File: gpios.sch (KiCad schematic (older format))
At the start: 28 parts, among them J1 TB_1X3, J2 TB_1X2, J3 TB_1X2, Q1 BC548, Q2 BC548, U1 4N25, U2 LM35, U3 4N25, U4 RELAY, U5 RELAY

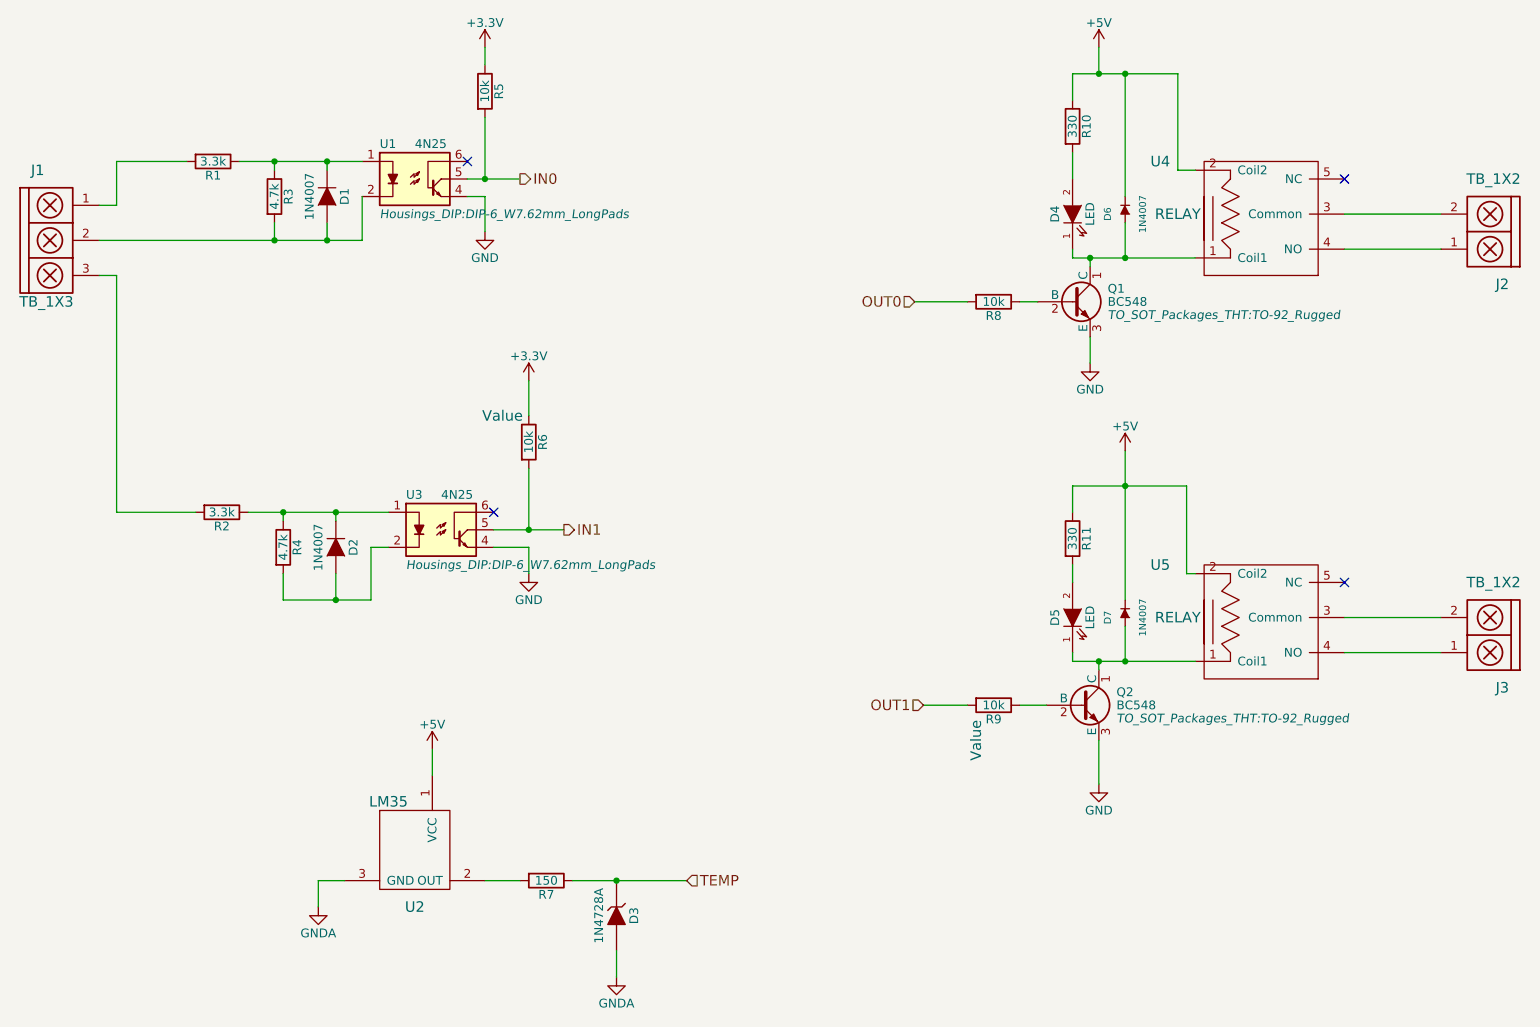
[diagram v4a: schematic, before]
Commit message: correcciones en esquemarico. ERC OK. Se crearon rotulos. PCB: replacing mas compacto
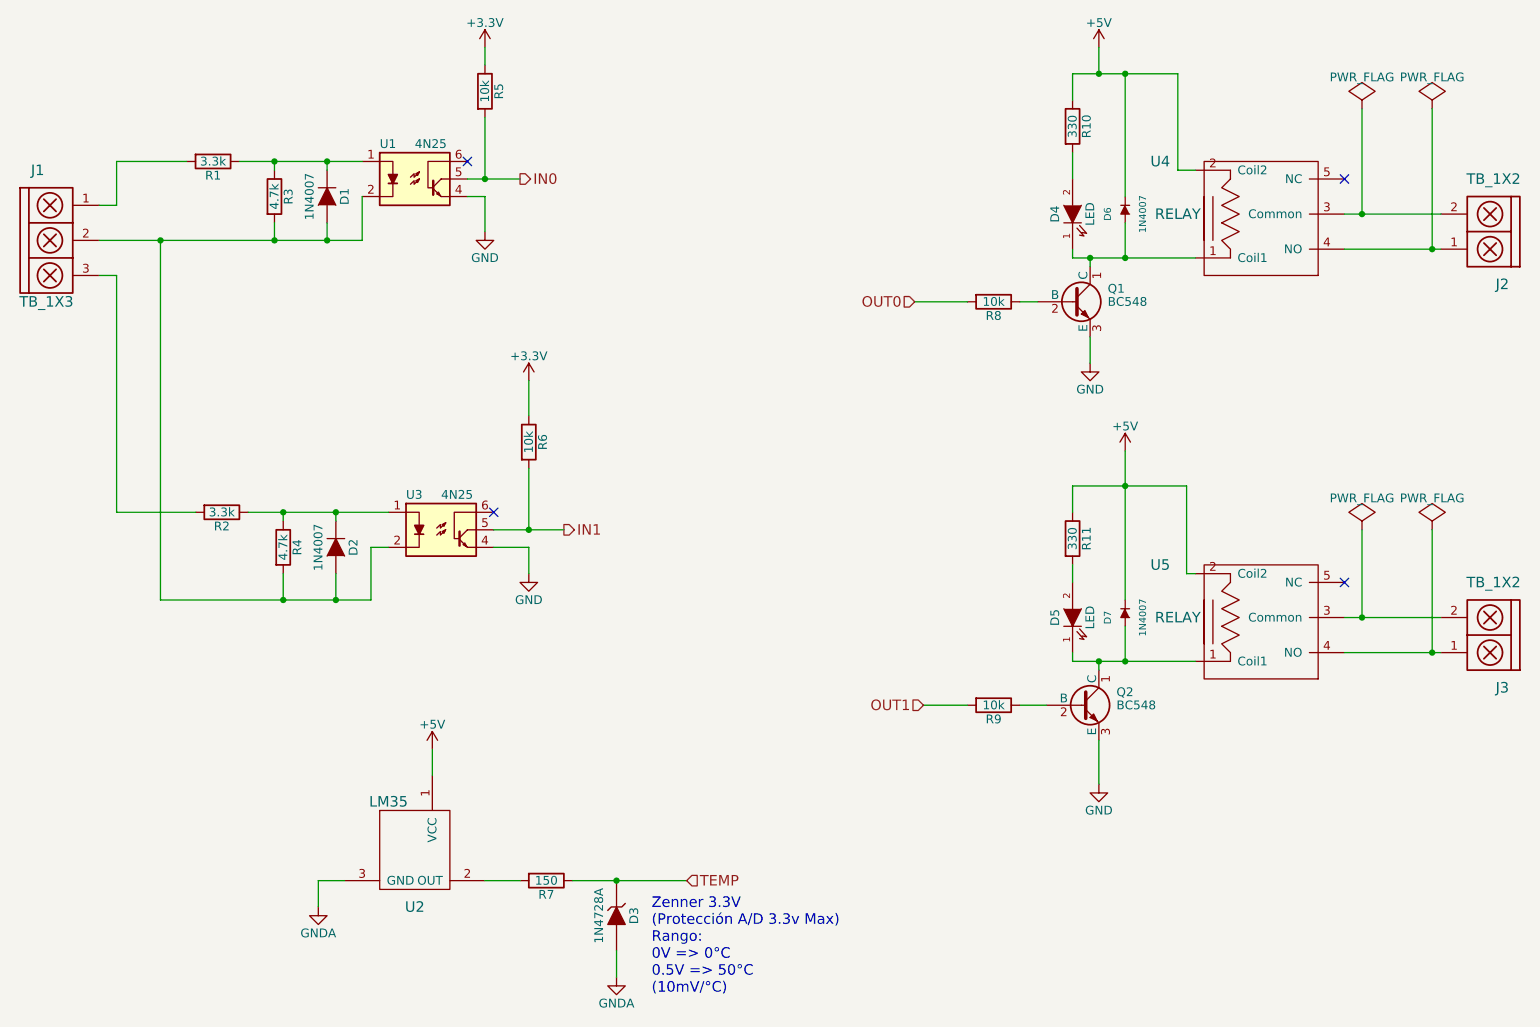
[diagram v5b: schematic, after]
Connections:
- net at D1.2 (A), J1.2, R3.2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: now also D2.2 (A), R4.2, U3.2
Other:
- note added: "Zenner 3.3V\n(Protección A/D 3.3v Max)\nRango: \n0V => 0°C\n0.5V => 50°C\n(10mV/°C)"
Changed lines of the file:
@@
 encoding utf-8
 Sheet 2 4
-Title "Poncho EDU-CIAA-NXP IoT"
+Title "Poncho EDU-CIAA-NXP IoT. GPIOs"
 Date "2016-11-09"
 Rev "1"
@@
 F 0 "Q1" H 7400 2525 50  0000 L CNN
 F 1 "BC548" H 7400 2450 50  0000 L CNN
-F 2 "TO_SOT_Packages_THT:TO-92_Rugged" H 7400 2375 50  0000 L CIN
+F 2 "TO_SOT_Packages_THT:TO-92_Rugged" H 7400 2375 50  0001 L CIN
 F 3 "" H 7200 2450 50  0000 L CNN
 	1    7200 2450
@@
 F 0 "Q2" H 7450 4825 50  0000 L CNN
 F 1 "BC548" H 7450 4750 50  0000 L CNN
-F 2 "TO_SOT_Packages_THT:TO-92_Rugged" H 7450 4675 50  0000 L CIN
+F 2 "TO_SOT_Packages_THT:TO-92_Rugged" H 7450 4675 50  0001 L CIN
 F 3 "" H 7250 4750 50  0000 L CNN
 	1    7250 4750
@@
 F 2 "Resistors_THT:Resistor_Horizontal_RM7mm" V 6680 4750 50  0001 C CNN
 F 3 "" H 6750 4750 50  0000 C CNN
-F 4 "Value" H 6950 4650 60  0000 C CNN "Digikey"
+F 4 "Value" H 6950 4650 60  0001 C CNN "Digikey"
 F 5 "Value" H 6750 4750 60  0001 C CNN "Fieldname"
 	1    6750 4750
@@
 F 0 "U1" H 3250 1950 50  0000 L CNN
 F 1 "4N25" H 3450 1950 50  0000 L CNN
-F 2 "Housings_DIP:DIP-6_W7.62mm_LongPads" H 3250 1550 50  0000 L CIN
+F 2 "Housings_DIP:DIP-6_W7.62mm_LongPads" H 3250 1550 50  0001 L CIN
 F 3 "" H 3450 1750 50  0000 L CNN
 	1    3450 1750
@@
 F 0 "U3" H 3400 3950 50  0000 L CNN
 F 1 "4N25" H 3600 3950 50  0000 L CNN
-F 2 "Housings_DIP:DIP-6_W7.62mm_LongPads" H 3400 3550 50  0000 L CIN
+F 2 "Housings_DIP:DIP-6_W7.62mm_LongPads" H 3400 3550 50  0001 L CIN
 F 3 "" H 3600 3750 50  0000 L CNN
 	1    3600 3750
@@
 F 2 "Resistors_THT:Resistor_Horizontal_RM7mm" V 4030 3250 50  0001 C CNN
 F 3 "" H 4100 3250 50  0000 C CNN
-F 4 "Value" H 3950 3400 60  0000 C CNN "Digikey"
+F 4 "Value" H 3950 3400 60  0001 C CNN "Digikey"
 F 5 "Value" H 4100 3250 60  0001 C CNN "Fieldname"
 	1    4100 3250
@@
 	3200 3850 3200 4150
 Wire Wire Line
-	3200 4150 2700 4150
+	3200 4150 2000 4150
 Wire Wire Line
 	2700 4150 2700 4000
@@
 	1    0    0    -1
 $EndComp
+Wire Wire Line
+	2000 4150 2000 2100
+Connection ~ 2000 2100
+Connection ~ 2700 4150
+Text Notes 4800 6400 0    60   ~ 0
+Zenner 3.3V\n(Protección A/D 3.3v Max)\nRango: \n0V => 0°C\n0.5V => 50°C\n(10mV/°C)
+$Comp
+L PWR_FLAG #FLG012
+U 1 1 582F3FFE
+P 8850 1350
+F 0 "#FLG012" H 8850 1445 50  0001 C CNN
+F 1 "PWR_FLAG" H 8850 1530 50  0000 C CNN
+F 2 "" H 8850 1350 50  0000 C CNN
+F 3 "" H 8850 1350 50  0000 C CNN
+	1    8850 1350
+	1    0    0    -1
+$EndComp
+$Comp
+L PWR_FLAG #FLG013
+U 1 1 582F404A
+P 9250 1350
+F 0 "#FLG013" H 9250 1445 50  0001 C CNN
+F 1 "PWR_FLAG" H 9250 1530 50  0000 C CNN
+F 2 "" H 9250 1350 50  0000 C CNN
+F 3 "" H 9250 1350 50  0000 C CNN
+	1    9250 1350
+	1    0    0    -1
+$EndComp
+Wire Wire Line
+	8850 1350 8850 1950
+Connection ~ 8850 1950
+Wire Wire Line
+	9250 1350 9250 2150
+Connection ~ 9250 2150
+$Comp
+L PWR_FLAG #FLG014
+U 1 1 582F58B7
+P 8850 3750
+F 0 "#FLG014" H 8850 3845 50  0001 C CNN
+F 1 "PWR_FLAG" H 8850 3930 50  0000 C CNN
+F 2 "" H 8850 3750 50  0000 C CNN
+F 3 "" H 8850 3750 50  0000 C CNN
+	1    8850 3750
+	1    0    0    -1
+$EndComp
+$Comp
+L PWR_FLAG #FLG015
+U 1 1 582F5903
+P 9250 3750
+F 0 "#FLG015" H 9250 3845 50  0001 C CNN
+F 1 "PWR_FLAG" H 9250 3930 50  0000 C CNN
+F 2 "" H 9250 3750 50  0000 C CNN
+F 3 "" H 9250 3750 50  0000 C CNN
+	1    9250 3750
+	1    0    0    -1
+$EndComp
+Wire Wire Line
+	8850 3750 8850 4250
+Connection ~ 8850 4250
+Wire Wire Line
+	9250 3750 9250 4450
+Connection ~ 9250 4450
 $EndSCHEMATC

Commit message: codigos digikey. falta terminar
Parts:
- D1, D2, D6, D7: Digikey# (none) -> 1N4007-TPMSTR-ND
- D4, D5: Digikey# (none) -> MV5054A3EL-ND
- Q1, Q2: Digikey# (none) -> BC548BTATB-ND
- R1: Digikey# (none) -> CF14JT3K30TR-ND; Fieldname Value -> (none)
- R10, R11: Digikey# (none) -> P330BATB-ND
- R2: Digikey# (none) -> CF14JT3K30TR-ND
- R3, R4: Digikey# (none) -> CF14JT4K70TR-ND
- R5, R6, R8, R9: Digikey# (none) -> CF14JT10K0TR-ND
- R7: Digikey# (none) -> CF14JT150RTR-ND
- U1, U3: Digikey# (none) -> 160-1300-5-ND; Fieldname (none) -> Value
- U2: Digikey# (none) -> LM35DZ/NOPB-ND
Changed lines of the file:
@@
 F 2 "TO_SOT_Packages_THT:TO-92_Rugged" H 7400 2375 50  0001 L CIN
 F 3 "" H 7200 2450 50  0000 L CNN
+F 4 "BC548BTATB-ND" H 7200 2450 60  0001 C CNN "Digikey#"
 	1    7200 2450
 	1    0    0    -1
@@
 F 2 "TO_SOT_Packages_THT:TO-92_Rugged" H 7450 4675 50  0001 L CIN
 F 3 "" H 7250 4750 50  0000 L CNN
+F 4 "BC548BTATB-ND" H 7250 4750 60  0001 C CNN "Digikey#"
 	1    7250 4750
 	1    0    0    -1
@@
 F 2 "Diodes_THT:Diode_DO-35_SOD27_Horizontal_RM10" H 7500 1950 60  0001 C CNN
 F 3 "" H 7500 1950 60  0000 C CNN
-F 4 "Value" H 7700 2000 60  0001 C CNN "Digikey"
-F 5 "Value" H 7500 1950 60  0001 C CNN "Fieldname"
+F 4 "1N4007-TPMSTR-ND" H 7500 1950 60  0001 C CNN "Digikey#"
+F 5 "Value" H 7700 2000 60  0001 C CNN "Digikey"
+F 6 "Value" H 7500 1950 60  0001 C CNN "Fieldname"
 	1    7500 1950
 	0    -1   -1   0
@@
 F 2 "Diodes_THT:Diode_DO-35_SOD27_Horizontal_RM10" H 7500 4250 60  0001 C CNN
 F 3 "" H 7500 4250 60  0000 C CNN
-F 4 "Value" H 7700 4300 60  0001 C CNN "Digikey"
-F 5 "Value" H 7500 4250 60  0001 C CNN "Fieldname"
+F 4 "1N4007-TPMSTR-ND" H 7500 4250 60  0001 C CNN "Digikey#"
+F 5 "Value" H 7700 4300 60  0001 C CNN "Digikey"
+F 6 "Value" H 7500 4250 60  0001 C CNN "Fieldname"
 	1    7500 4250
 	0    -1   -1   0
@@
 F 2 "LEDs:LED-3MM" H 7200 1950 50  0001 C CNN
 F 3 "" H 7200 1950 50  0000 C CNN
+F 4 "MV5054A3EL-ND" H 7200 1950 60  0001 C CNN "Digikey#"
 	1    7200 1950
 	0    -1   -1   0
@@
 F 2 "LEDs:LED-3MM" H 7200 4250 50  0001 C CNN
 F 3 "" H 7200 4250 50  0000 C CNN
+F 4 "MV5054A3EL-ND" H 7200 4250 60  0001 C CNN "Digikey#"
 	1    7200 4250
 	0    -1   -1   0
@@
 F 2 "Resistors_THT:Resistor_Horizontal_RM7mm" V 7130 1450 50  0001 C CNN
 F 3 "" H 7200 1450 50  0000 C CNN
-F 4 "Value" H 7050 1650 60  0001 C CNN "Digikey"
-F 5 "Value" H 7200 1450 60  0001 C CNN "Fieldname"
+F 4 "P330BATB-ND" H 7200 1450 60  0001 C CNN "Digikey#"
+F 5 "Value" H 7050 1650 60  0001 C CNN "Digikey"
+F 6 "Value" H 7200 1450 60  0001 C CNN "Fieldname"
 	1    7200 1450
 	1    0    0    -1
@@
 F 2 "Resistors_THT:Resistor_Horizontal_RM7mm" V 7130 3800 50  0001 C CNN
 F 3 "" H 7200 3800 50  0000 C CNN
-F 4 "Value" H 7050 3950 60  0001 C CNN "Digikey"
-F 5 "Value" H 7200 3800 60  0001 C CNN "Fieldname"
+F 4 "P330BATB-ND" H 7200 3800 60  0001 C CNN "Digikey#"
+F 5 "Value" H 7050 3950 60  0001 C CNN "Digikey"
+F 6 "Value" H 7200 3800 60  0001 C CNN "Fieldname"
 	1    7200 3800
 	1    0    0    -1
@@
 F 2 "Resistors_THT:Resistor_Horizontal_RM7mm" V 6680 2450 50  0001 C CNN
 F 3 "" H 6750 2450 50  0000 C CNN
-F 4 "Value" H 6900 2250 60  0001 C CNN "Digikey"
-F 5 "Value" H 6750 2450 60  0001 C CNN "Fieldname"
+F 4 "CF14JT10K0TR-ND" H 6750 2450 60  0001 C CNN "Digikey#"
+F 5 "Value" H 6900 2250 60  0001 C CNN "Digikey"
+F 6 "Value" H 6750 2450 60  0001 C CNN "Fieldname"
 	1    6750 2450
 	0    1    1    0
@@
 F 2 "Resistors_THT:Resistor_Horizontal_RM7mm" V 6680 4750 50  0001 C CNN
 F 3 "" H 6750 4750 50  0000 C CNN
-F 4 "Value" H 6950 4650 60  0001 C CNN "Digikey"
-F 5 "Value" H 6750 4750 60  0001 C CNN "Fieldname"
+F 4 "CF14JT10K0TR-ND" H 6750 4750 60  0001 C CNN "Digikey#"
+F 5 "Value" H 6950 4650 60  0001 C CNN "Digikey"
+F 6 "Value" H 6750 4750 60  0001 C CNN "Fieldname"
 	1    6750 4750
 	0    1    1    0
@@
 F 2 "Housings_DIP:DIP-6_W7.62mm_LongPads" H 3250 1550 50  0001 L CIN
 F 3 "" H 3450 1750 50  0000 L CNN
+F 4 "160-1300-5-ND" H 3450 1750 60  0001 C CNN "Digikey#"
+F 5 "Value" H 3450 1750 60  0001 C CNN "Fieldname"
 	1    3450 1750
 	1    0    0    -1
@@
 F 2 "Housings_DIP:DIP-6_W7.62mm_LongPads" H 3400 3550 50  0001 L CIN
 F 3 "" H 3600 3750 50  0000 L CNN
+F 4 "Value" H 3600 3750 60  0001 C CNN "Fieldname"
+F 5 "160-1300-5-ND" H 3600 3750 60  0001 C CNN "Digikey#"
 	1    3600 3750
 	1    0    0    -1
@@
 F 2 "Resistors_THT:Resistor_Horizontal_RM7mm" V 3780 1250 50  0001 C CNN
 F 3 "" H 3850 1250 50  0000 C CNN
-F 4 "Value" H 3700 1400 60  0001 C CNN "Digikey"
-F 5 "Value" H 3850 1250 60  0001 C CNN "Fieldname"
+F 4 "CF14JT10K0TR-ND" H 3850 1250 60  0001 C CNN "Digikey#"
+F 5 "Value" H 3700 1400 60  0001 C CNN "Digikey"
+F 6 "Value" H 3850 1250 60  0001 C CNN "Fieldname"
 	1    3850 1250
 	1    0    0    -1
@@
 F 2 "Resistors_THT:Resistor_Horizontal_RM7mm" V 2230 1650 50  0001 C CNN
 F 3 "" H 2300 1650 50  0000 C CNN
-F 4 "Value" H 2300 1650 60  0001 C CNN "Fieldname"
+F 4 "CF14JT3K30TR-ND" H 2300 1650 60  0001 C CNN "Digikey#"
 	1    2300 1650
 	0    1    1    0
@@
 F 2 "Resistors_THT:Resistor_Horizontal_RM7mm" V 2580 1850 50  0001 C CNN
 F 3 "" H 2650 1850 50  0000 C CNN
-F 4 "Value" H 2650 1850 60  0001 C CNN "Fieldname"
+F 4 "CF14JT4K70TR-ND" H 2650 1850 60  0001 C CNN "Digikey#"
+F 5 "Value" H 2650 1850 60  0001 C CNN "Fieldname"
 	1    2650 1850
 	1    0    0    -1
@@
 F 2 "Diodes_THT:Diode_DO-35_SOD27_Horizontal_RM10" H 2950 1850 50  0001 C CNN
 F 3 "" H 2950 1850 50  0000 C CNN
-F 4 "Value" H 2600 1800 60  0001 C CNN "Digikey"
-F 5 "Value" H 2950 1850 60  0001 C CNN "Fieldname"
+F 4 "1N4007-TPMSTR-ND" H 2950 1850 60  0001 C CNN "Digikey#"
+F 5 "Value" H 2600 1800 60  0001 C CNN "Digikey"
+F 6 "Value" H 2950 1850 60  0001 C CNN "Fieldname"
 	1    2950 1850
 	0    1    1    0
@@
 F 2 "Resistors_THT:Resistor_Horizontal_RM7mm" V 4030 3250 50  0001 C CNN
 F 3 "" H 4100 3250 50  0000 C CNN
-F 4 "Value" H 3950 3400 60  0001 C CNN "Digikey"
-F 5 "Value" H 4100 3250 60  0001 C CNN "Fieldname"
+F 4 "CF14JT10K0TR-ND" H 4100 3250 60  0001 C CNN "Digikey#"
+F 5 "Value" H 3950 3400 60  0001 C CNN "Digikey"
+F 6 "Value" H 4100 3250 60  0001 C CNN "Fieldname"
 	1    4100 3250
 	1    0    0    -1
@@
 F 2 "Resistors_THT:Resistor_Horizontal_RM7mm" V 2630 3850 50  0001 C CNN
 F 3 "" H 2700 3850 50  0000 C CNN
-F 4 "Value" H 2700 3850 60  0001 C CNN "Fieldname"
+F 4 "CF14JT4K70TR-ND" H 2700 3850 60  0001 C CNN "Digikey#"
+F 5 "Value" H 2700 3850 60  0001 C CNN "Fieldname"
 	1    2700 3850
 	1    0    0    -1
@@
 F 2 "Resistors_THT:Resistor_Horizontal_RM7mm" V 2280 3650 50  0001 C CNN
 F 3 "" H 2350 3650 50  0000 C CNN
-F 4 "Value" H 2350 3650 60  0001 C CNN "Fieldname"
+F 4 "CF14JT3K30TR-ND" H 2350 3650 60  0001 C CNN "Digikey#"
+F 5 "Value" H 2350 3650 60  0001 C CNN "Fieldname"
 	1    2350 3650
 	0    1    1    0
@@
 F 2 "Diodes_THT:Diode_DO-35_SOD27_Horizontal_RM10" H 3000 3850 50  0001 C CNN
 F 3 "" H 3000 3850 50  0000 C CNN
-F 4 "Value" H 3450 3800 60  0001 C CNN "Digikey"
-F 5 "Value" H 3000 3850 60  0001 C CNN "Fieldname"
+F 4 "1N4007-TPMSTR-ND" H 3000 3850 60  0001 C CNN "Digikey#"
+F 5 "Value" H 3450 3800 60  0001 C CNN "Digikey"
+F 6 "Value" H 3000 3850 60  0001 C CNN "Fieldname"
 	1    3000 3850
 	0    1    1    0
@@
 F 2 "TO_SOT_Packages_THT:TO-92_Rugged" H 3450 5900 60  0001 C CNN
 F 3 "" H 3450 5900 60  0001 C CNN
-F 4 "Value" H 3450 5900 60  0001 C CNN "Fieldname"
+F 4 "LM35DZ/NOPB-ND" H 3450 5900 60  0001 C CNN "Digikey#"
+F 5 "Value" H 3450 5900 60  0001 C CNN "Fieldname"
 	1    3450 5900
 	1    0    0    -1
@@
 F 2 "Resistors_THT:Resistor_Horizontal_RM7mm" V 4130 5750 50  0001 C CNN
 F 3 "" H 4200 5750 50  0000 C CNN
-F 4 "Value" H 4200 5750 60  0001 C CNN "Fieldname"
-F 5 "Value" H 4000 5650 60  0001 C CNN "Digikey"
+F 4 "CF14JT150RTR-ND" H 4200 5750 60  0001 C CNN "Digikey#"
+F 5 "Value" H 4200 5750 60  0001 C CNN "Fieldname"
+F 6 "Value" H 4000 5650 60  0001 C CNN "Digikey"
 	1    4200 5750
 	0    1    1    0

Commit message: se acomodaron las referencias de los componentes, se pusieron algunos modelos 3d
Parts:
- D3: Digikey# (none) -> 1N4728AVSTR-ND
- J1: Digikey# (none) -> ED2610-ND
- J2, J3: Digikey# (none) -> ED2609-ND
- U4, U5: Digikey# (none) -> PB2029-ND
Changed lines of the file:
@@
 F 2 "ponchoeduciaaiot:bornier3" H 1250 2050 60  0001 C CNN
 F 3 "" H 1250 2050 60  0000 C CNN
+F 4 "ED2610-ND" H 1300 2000 60  0001 C CNN "Digikey#"
 	1    1300 2000
 	1    0    0    -1
@@
 F 2 "ponchoeduciaaiot:bornier2" H 9600 2100 60  0001 C CNN
 F 3 "" H 9600 2100 60  0000 C CNN
+F 4 "ED2609-ND" H 9650 2050 60  0001 C CNN "Digikey#"
 	1    9650 2050
 	-1   0    0    1
@@
 F 2 "ponchoeduciaaiot:bornier2" H 9600 4400 60  0001 C CNN
 F 3 "" H 9600 4400 60  0000 C CNN
+F 4 "ED2609-ND" H 9650 4350 60  0001 C CNN "Digikey#"
 	1    9650 4350
 	-1   0    0    1
@@
 F 2 "ponchoeduciaaiot:Relay5vSI" H 7700 1650 60  0001 C CNN
 F 3 "" H 7700 1650 60  0001 C CNN
+F 4 "PB2029-ND" H 7700 1650 60  0001 C CNN "Digikey#"
 	1    7700 1650
 	-1   0    0    1
@@
 F 2 "ponchoeduciaaiot:Relay5vSI" H 7700 3950 60  0001 C CNN
 F 3 "" H 7700 3950 60  0001 C CNN
+F 4 "PB2029-ND" H 7700 3950 60  0001 C CNN "Digikey#"
 	1    7700 3950
 	-1   0    0    1
@@
 F 2 "Diodes_THT:Diode_DO-35_SOD27_Horizontal_RM10" H 4600 5950 50  0001 C CNN
 F 3 "" H 4600 5950 50  0000 C CNN
-F 4 "Value" H 4800 6100 60  0001 C CNN "Digikey"
-F 5 "Value" H 4600 5950 60  0001 C CNN "Fieldname"
+F 4 "1N4728AVSTR-ND" H 4600 5950 60  0001 C CNN "Digikey#"
+F 5 "Value" H 4800 6100 60  0001 C CNN "Digikey"
+F 6 "Value" H 4600 5950 60  0001 C CNN "Fieldname"
 	1    4600 5950
 	0    1    1    0

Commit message: cargar campos kicost OK
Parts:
- D1, D2, D6, D7: Digikey Value -> (none); Fieldname Value -> (none); Manf (none) -> Micro Commercial Co; Manf# (none) -> 1N4007-TP
- D3: Digikey Value -> (none); Fieldname Value -> (none); Manf (none) -> Vishay Semiconductor Diodes Division; Manf# (none) -> 1N4728A-TR
- D4, D5: Manf (none) -> Everlight Electronics Co Ltd; Manf# (none) -> MV5054A3
- J1: Manf (none) -> On Shore Technology Inc.; Manf# (none) -> OSTTC032162
- J2, J3: Manf (none) -> On Shore Technology Inc.; Manf# (none) -> OSTTC022162
- Q1, Q2: Manf (none) -> Fairchild Semiconductor; Manf# (none) -> BC548BTA
- R1: Manf (none) -> Stackpole Electronics Inc.; Manf# (none) -> CF14JT3K30
- R10, R11: Digikey Value -> (none); Fieldname Value -> (none); Manf (none) -> Panasonic Electronic Components; Manf# (none) -> P330BATB-ND
- R2: Fieldname Value -> (none); Manf (none) -> Stackpole Electronics Inc.; Manf# (none) -> CF14JT3K30
- R3, R4: Fieldname Value -> (none); Manf (none) -> Stackpole Electronics Inc.; Manf# (none) -> CF14JT4K70
- R5, R6, R8: Fieldname Value -> (none); Manf (none) -> Stackpole Electronics Inc.; Manf# (none) -> CF14JT10K0
- R7: Digikey Value -> (none); Fieldname Value -> (none); Manf (none) -> Stackpole Electronics Inc.; Manf# (none) -> CF14JT150R
- R9: Digikey Value -> (none); Fieldname Value -> (none); Manf (none) -> Stackpole Electronics Inc.; Manf# (none) -> CF14JT10K0
- U1, U3: Fieldname Value -> (none); Manf (none) -> Lite-On Inc.; Manf# (none) -> 4N25
- U2: Fieldname Value -> (none); Manf (none) -> Texas Instruments; Manf# (none) -> LM35DZ/NOPB
- U4, U5: Manf (none) -> TE Connectivity Potter & Brumfield Relays; Manf# (none) -> ORWH-SH-112D1F,000
